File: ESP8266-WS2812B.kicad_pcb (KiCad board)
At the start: 2 copper layers, 60 x 50 mm, 34 parts, among them J1 USB_B_Micro, J2 Alternate_Power_Input, J3 Conn_02x03_Odd_Even, J4 Conn_01x03, Q1 Q_NPN_BEC, SW1 SW_Push, U1 ESP-12F, U2 AP2114HA-3.3

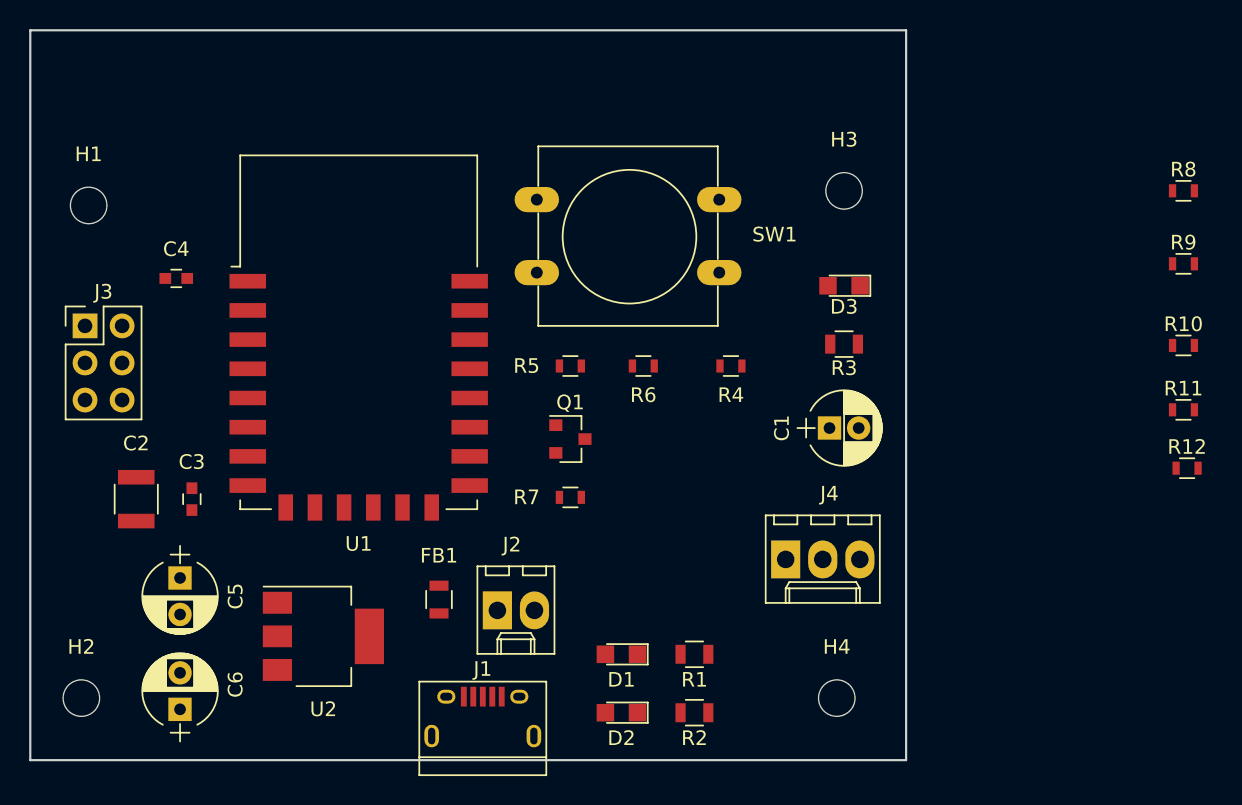
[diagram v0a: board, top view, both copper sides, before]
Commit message: Arranged components and drawn PCB outline
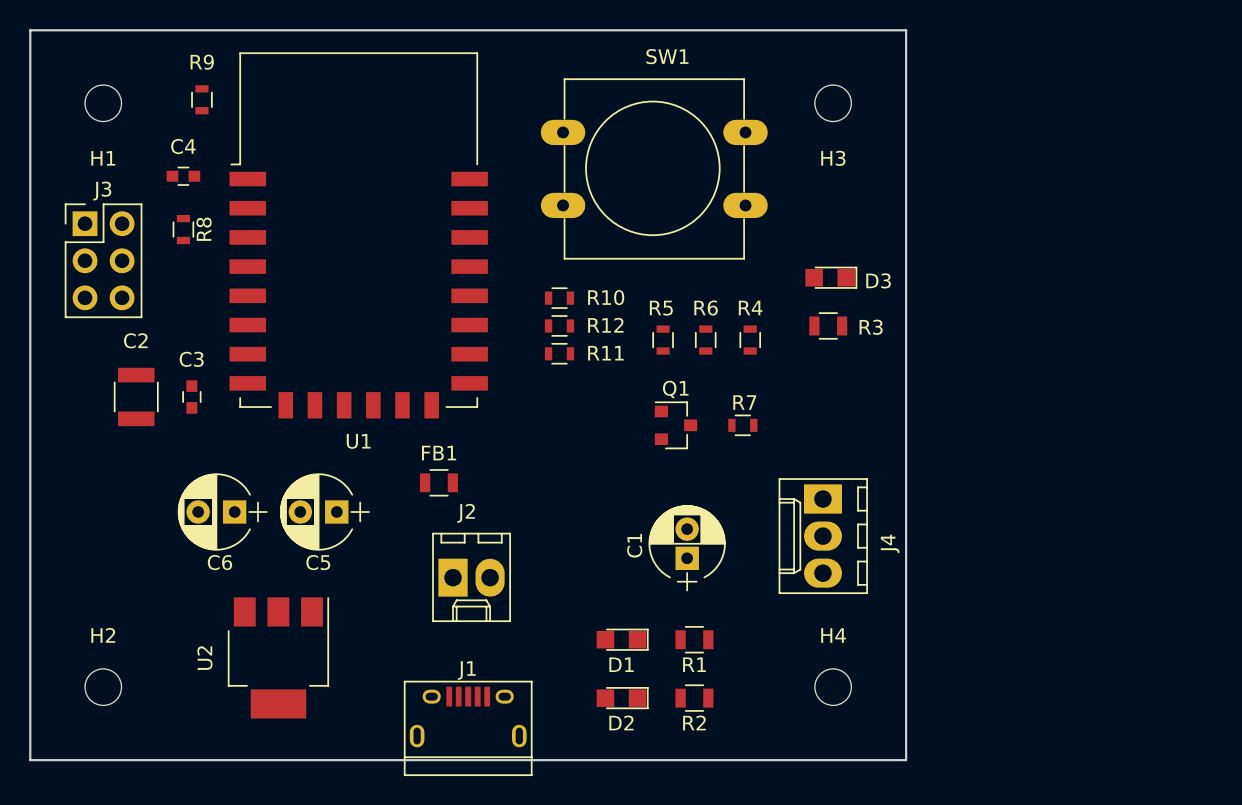
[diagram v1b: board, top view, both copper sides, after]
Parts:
- moved R8 68.6 mm to (110.5, 113.7), turned to 270 degrees
- moved R9 68.2 mm to (111.8, 104.8), turned to 270 degrees
- moved R12 44.1 mm to (136.3, 120.3), turned to 180 degrees
- moved R11 42.9 mm to (136.3, 122.2)
- moved R10 42.9 mm to (136.3, 118.3), turned to 180 degrees
- moved SW1 14.3 mm to (149.0, 112.0), turned to 180 degrees
- moved C6 14.0 mm to (114.0, 133.0), turned to 180 degrees
- moved C1 13.2 mm to (145.0, 136.2), turned to 90 degrees
- moved R7 12.8 mm to (148.8, 127.1)
- moved C5 11.7 mm to (121.0, 133.0), turned to 180 degrees
- moved FB1 8.00 mm to (128.0, 131.0), turned to 0 degrees
- moved Q1 7.30 mm to (144.2, 127.1)
- moved H1 7.07 mm to (105.0, 105.0)
- moved C4 7.02 mm to (110.5, 110.0)
- moved C2 7.00 mm to (107.3, 125.1)
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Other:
- net class Default: clearance 0.2 -> 0.25
- rule trace_clearance: 0.2 -> 0.25

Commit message: Added copper fill/no fill zones and finished first pass of connecting all nets.
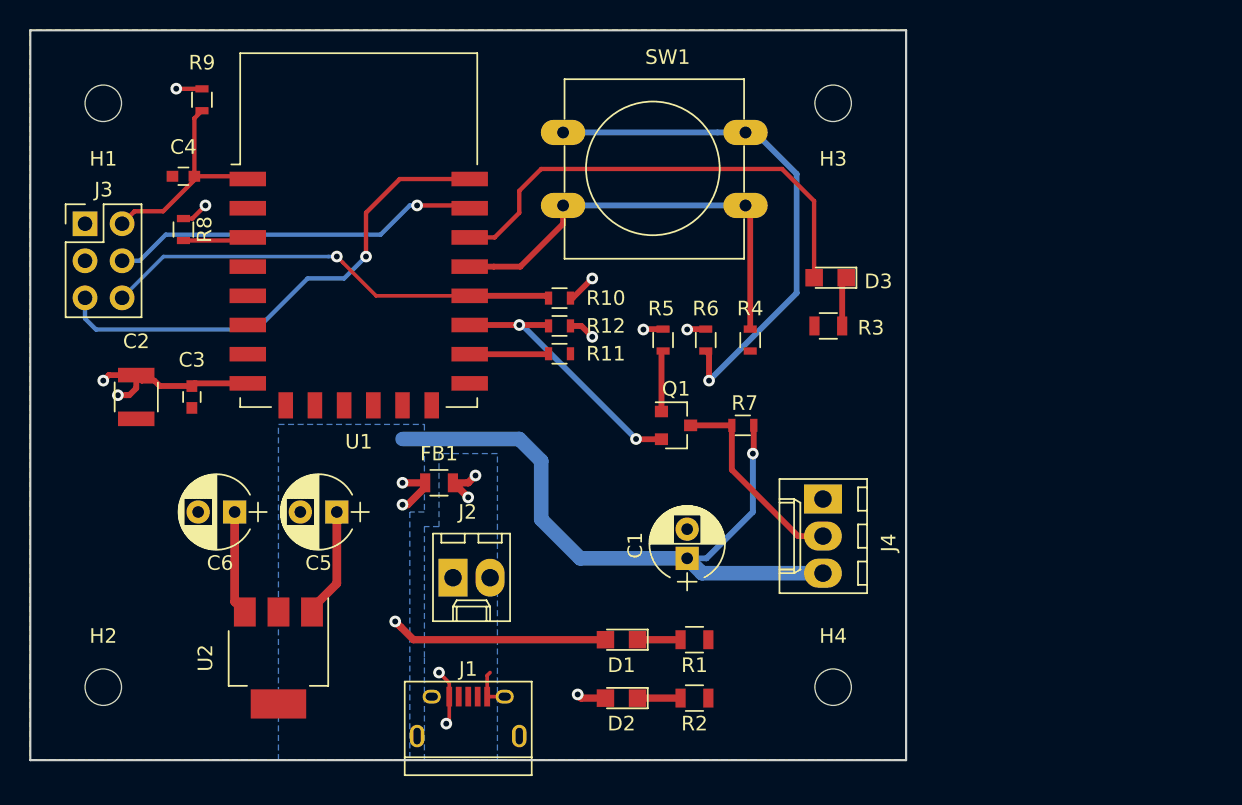
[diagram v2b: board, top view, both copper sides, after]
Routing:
- net +5V: track 0.00 -> 73.1 mm, vias 0 -> 4
- net /Button_Open_Side: track 0.00 -> 35.9 mm, vias 0 -> 1
- net /TXD: track 0.00 -> 34.1 mm, vias 0 -> 1
- net /ESP8266/GPIO5: track 0.00 -> 32.6 mm
- net +3V3: track 0.00 -> 32.1 mm, vias 0 -> 9
- net /GPIO0: track 0.00 -> 31.6 mm, vias 0 -> 1
- net /ESP8266/GPIO4: track 0.00 -> 30.0 mm
- net /RXD: track 0.00 -> 25.5 mm, vias 0 -> 1
- net /ESP8266/GPIO2: track 0.00 -> 18.4 mm, vias 0 -> 2
- net /~RST: track 0.00 -> 14.9 mm
- net /DATA: track 0.00 -> 14.0 mm
- net /5V_Input: track 0.00 -> 7.09 mm, vias 0 -> 4
- net /ESP8266/GPIO15: track 0.00 -> 5.42 mm
- net /ESP8266/EN: track 0.00 -> 4.50 mm
- net /Level_Shift_Base: track 0.00 -> 4.19 mm
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- added copper zone on B.Cu, net +3V3
- added copper zone on B.Cu, net +5V
- added copper zone on B.Cu, net /5V_Input
- added copper zone on F.Cu, net GND

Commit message: Generated gerbers and allowed GND copper flow to flow under the ESP module.
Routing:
- net GND: track 2.93 -> 6.27 mm
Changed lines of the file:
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@@
     (thickness 1.6)
     (drawings 4)
-    (tracks 159)
+    (tracks 161)
     (zones 0)
     (modules 34)
@@
     (visible_elements FFFFFF7F)
     (pcbplotparams
-      (layerselection 0x010fc_ffffffff)
+      (layerselection 0x010f0_ffffffff)
       (usegerberextensions false)
       (usegerberattributes false)
@@
       (outputformat 1)
       (mirror false)
-      (drillshape 1)
+      (drillshape 0)
       (scaleselection 1)
-      (outputdirectory ""))
+      (outputdirectory "gerbers/"))
   )
   (net 0 "")
@@
   (segment (start 131.3 144.2) (end 131.5 144) (width 0.25) (layer F.Cu) (net 1))
   (segment (start 131.3 145.65) (end 132.5 145.65) (width 0.25) (layer F.Cu) (net 1))
+  (segment (start 128.45 124.19) (end 127.26 123) (width 0.4) (layer F.Cu) (net 1))
+  (segment (start 130.1 124.19) (end 128.45 124.19) (width 0.4) (layer F.Cu) (net 1))
   (segment (start 119.3 139.6) (end 119.3 139.85) (width 0.6) (layer F.Cu) (net 2))
   (segment (start 121 137.9) (end 119.3 139.6) (width 0.6) (layer F.Cu) (net 2))

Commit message: Added PCB/author information on bottom silkscreen layer and added some connector information on top silkscreen layer.
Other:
- board text added: "5V"
- board text added: "Author:"
- board text added: "Connor Driscoll"
- board text added: "ESP8266 LED"
- board text added: "PCB:"
- board text added: "Rev A"
- board text added: "Revision:"
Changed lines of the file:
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@@
   (general
     (thickness 1.6)
-    (drawings 4)
+    (drawings 39)
     (tracks 161)
     (zones 0)
@@
     (pad 1 np_thru_hole circle (at 0 0) (size 2.5 2.5) (drill 2.5) (layers *.Cu *.Mask))
   )
+  (gr_text "Rev A" (at 124.2 106.5) (layer B.SilkS)
+    (effects (font (size 1 1) (thickness 0.2)) (justify mirror))
+  )
+  (gr_text "Connor Driscoll" (at 120.6 104.4) (layer B.SilkS)
+    (effects (font (size 1 1) (thickness 0.2)) (justify mirror))
+  )
+  (gr_text "ESP8266 LED" (at 121 102.5) (layer B.SilkS)
+    (effects (font (size 1 1) (thickness 0.15)) (justify mirror))
+  )
+  (gr_line (start 133.9 103.4) (end 114.4 103.4) (layer B.SilkS) (width 0.2))
+  (gr_line (start 114.4 105.4) (end 133.9 105.4) (layer B.SilkS) (width 0.2))
+  (gr_line (start 126.6 101.4) (end 126.6 107.5) (layer B.SilkS) (width 0.2))
+  (gr_text Revision: (at 130.1 106.4) (layer B.SilkS)
+    (effects (font (size 1 1) (thickness 0.2)) (justify mirror))
+  )
+  (gr_text PCB: (at 131.5 102.4) (layer B.SilkS)
+    (effects (font (size 1 1) (thickness 0.2)) (justify mirror))
+  )
+  (gr_text Author: (at 130.7 104.4) (layer B.SilkS)
+    (effects (font (size 1 1) (thickness 0.2)) (justify mirror))
+  )
+  (gr_line (start 133.9 101.4) (end 114.4 101.4) (layer B.SilkS) (width 0.2))
+  (gr_line (start 133.9 107.5) (end 133.9 101.4) (layer B.SilkS) (width 0.2))
+  (gr_line (start 114.4 107.5) (end 133.9 107.5) (layer B.SilkS) (width 0.2))
+  (gr_line (start 114.4 101.4) (end 114.4 107.5) (layer B.SilkS) (width 0.2))
+  (gr_line (start 134.3 139.1) (end 134.7 139.1) (layer F.SilkS) (width 0.2))
+  (gr_line (start 134.1 138.7) (end 134.9 138.7) (layer F.SilkS) (width 0.2))
+  (gr_line (start 133.9 138.3) (end 135.2 138.3) (layer F.SilkS) (width 0.2))
+  (gr_line (start 134.5 137.4) (end 134.5 138.3) (layer F.SilkS) (width 0.2))
+  (gr_line (start 132.8 137.4) (end 134.5 137.4) (layer F.SilkS) (width 0.2))
+  (gr_line (start 127.6 137.6) (end 125.8 137.6) (layer F.SilkS) (width 0.2))
+  (gr_text 5V (at 124.7 137.6) (layer F.SilkS)
+    (effects (font (size 1 1) (thickness 0.2)))
+  )
+  (gr_text 5V (at 151.2 141.8) (layer F.SilkS)
+    (effects (font (size 1 1) (thickness 0.2)))
+  )
+  (gr_line (start 151.3 139.7) (end 151.3 140.9) (layer F.SilkS) (width 0.2))
+  (gr_line (start 152.3 139.7) (end 151.3 139.7) (layer F.SilkS) (width 0.2))
+  (gr_line (start 154.3 139.7) (end 152.3 139.7) (layer F.SilkS) (width 0.2))
+  (gr_line (start 154.3 138.3) (end 154.3 139.7) (layer F.SilkS) (width 0.2))
+  (gr_line (start 102 108.9) (end 102.6 108.9) (layer F.SilkS) (width 0.2))
+  (gr_line (start 101.8 109.3) (end 102.8 109.3) (layer F.SilkS) (width 0.2))
+  (gr_line (start 101.6 109.7) (end 103 109.7) (layer F.SilkS) (width 0.2))
+  (gr_line (start 102.3 110.4) (end 102.3 109.7) (layer F.SilkS) (width 0.2))
+  (gr_line (start 103.7 110.4) (end 102.3 110.4) (layer F.SilkS) (width 0.2))
+  (gr_line (start 103.7 112.3) (end 103.7 110.4) (layer F.SilkS) (width 0.2))
+  (gr_line (start 153.9 127.5) (end 154.8 127.5) (layer F.SilkS) (width 0.2))
+  (gr_line (start 153.6 128) (end 155.1 128) (layer F.SilkS) (width 0.2))
+  (gr_line (start 153.4 128.5) (end 155.3 128.5) (layer F.SilkS) (width 0.2))
+  (gr_line (start 154.3 131.1) (end 154.3 128.6) (layer F.SilkS) (width 0.2))
   (gr_line (start 160 100) (end 100 100) (layer Edge.Cuts) (width 0.15))
   (gr_line (start 160 150) (end 160 100) (layer Edge.Cuts) (width 0.15))
